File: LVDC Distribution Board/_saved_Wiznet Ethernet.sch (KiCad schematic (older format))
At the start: 51 parts, among them J601 RB1-125BAG1A, U601 W5500, Y601 25MHz

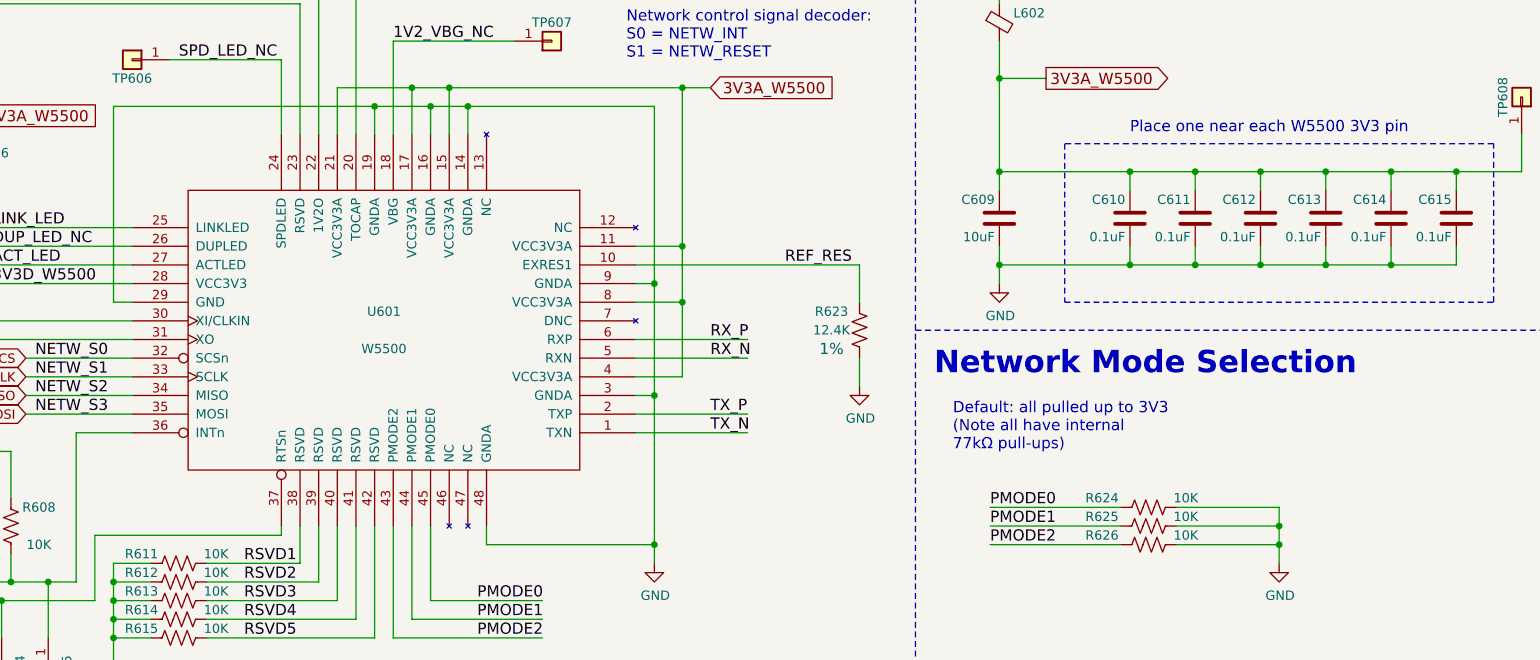
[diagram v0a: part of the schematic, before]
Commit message: Added 2 rj45 jacks, LEFT: MOSFET pkg, current sense traces, tidy planes and routing
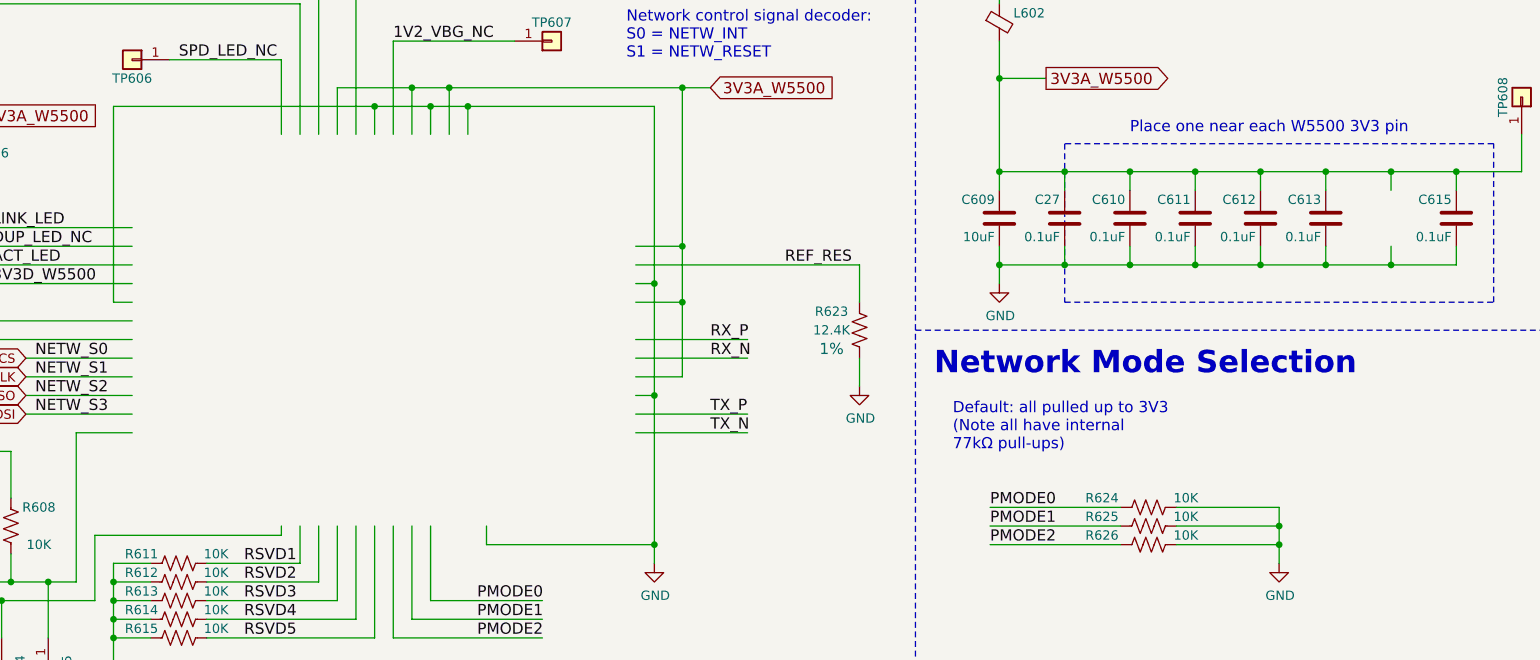
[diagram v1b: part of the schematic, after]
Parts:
- removed C614: 0.1uF, Resistors_SMD:R_0402, symbol Device:C
- removed U601: W5500, Package_QFP:LQFP-48_7x7mm_P0.5mm, symbol LVDC-Library:W5500
- added C27: 0.1uF, Resistors_SMD:R_0402, symbol Device:C
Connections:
- wire segments 215 -> 219
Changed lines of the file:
@@
-$EndComp
-$Comp
-L LVDC-Library:W5500 U601
-U 1 1 59E0CCFB
-P 4850 2900
-F 0 "U601" H 4850 2800 50  0000 C CNN
-F 1 "W5500" H 4850 3000 50  0000 C CNN
-F 2 "Package_QFP:LQFP-48_7x7mm_P0.5mm" H 4850 2900 50  0001 C CNN
-F 3 "" H 4850 2900 50  0001 C CNN
-F 4 "W5500" H 4850 2900 60  0001 C CNN "Mfg. Part Num"
-F 5 "WIZnet" H 4850 2900 60  0001 C CNN "Mfg. Name"
-F 6 "1278-1021-ND" H 4850 2900 60  0001 C CNN "Vendor Part Num"
-	1    4850 2900
-	-1   0    0    1
 $EndComp
 $Comp
@@
 F 3 "" H 9900 2300 50  0001 C CNN
 	1    9900 2300
-	-1   0    0    -1
-$EndComp
-$Comp
-L Device:C C614
-U 1 1 59E2A80A
-P 10250 2300
-F 0 "C614" H 10275 2400 50  0000 L CNN
-F 1 "0.1uF" H 10275 2200 50  0000 L CNN
-F 2 "Resistors_SMD:R_0402" H 10288 2150 50  0001 C CNN
-F 3 "" H 10250 2300 50  0001 C CNN
-	1    10250 2300
 	-1   0    0    -1
 $EndComp
@@
 	8150 1350 8150 1550
 Wire Wire Line
-	8150 2050 8850 2050
+	8150 2050 8500 2050
 Wire Wire Line
 	10600 2050 10600 2150
@@
 	8150 2450 8150 2550
 Wire Wire Line
-	8150 2550 8850 2550
+	8150 2550 8500 2550
 Wire Wire Line
 	10600 2550 10600 2450
@@
 Wire Wire Line
 	750  2850 3500 2850
+$Comp
+L Device:C C27
+U 1 1 5CD46454
+P 8500 2300
+F 0 "C27" H 8525 2400 50  0000 L CNN
+F 1 "0.1uF" H 8525 2200 50  0000 L CNN
+F 2 "Resistors_SMD:R_0402" H 8538 2150 50  0001 C CNN
+F 3 "" H 8500 2300 50  0001 C CNN
+	1    8500 2300
+	-1   0    0    -1
+$EndComp
+Wire Wire Line
+	8500 2150 8500 2050
+Connection ~ 8500 2050
+Wire Wire Line
+	8500 2050 8850 2050
+Wire Wire Line
+	8500 2450 8500 2550
+Connection ~ 8500 2550
+Wire Wire Line
+	8500 2550 8850 2550
 $EndSCHEMATC
